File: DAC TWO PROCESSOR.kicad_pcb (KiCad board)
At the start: 4 copper layers, 94 x 50.8 mm, 100 parts, among them J1 CONN_20, J2 CONN_10x2, J3 CONN_10, U1 ADP5070, U10 LT1964-SD, U11 SM78L05, U12 SM79L05, U2 REG113-3.3, U3 XX MHz, U4 ADP7118, U5 AT25160B, U6 ADP7182, U7 STM32F7xx, U8 LT1763CS8, U9 LT1763CS8

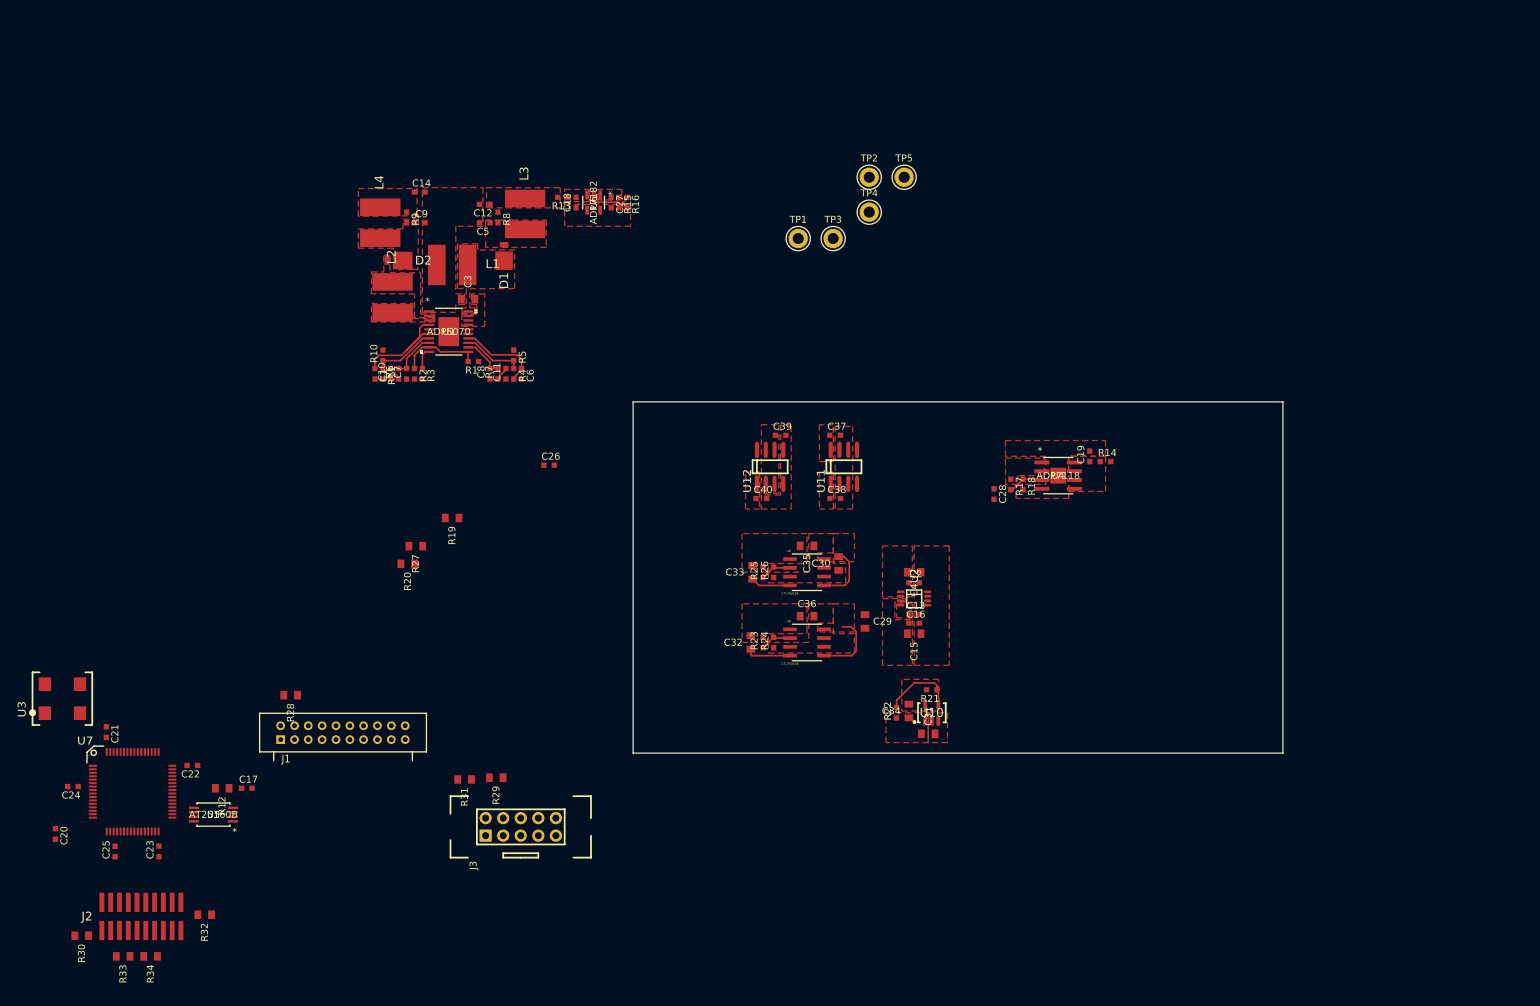
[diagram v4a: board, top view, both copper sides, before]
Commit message: Layout and placement of most switchers complete.
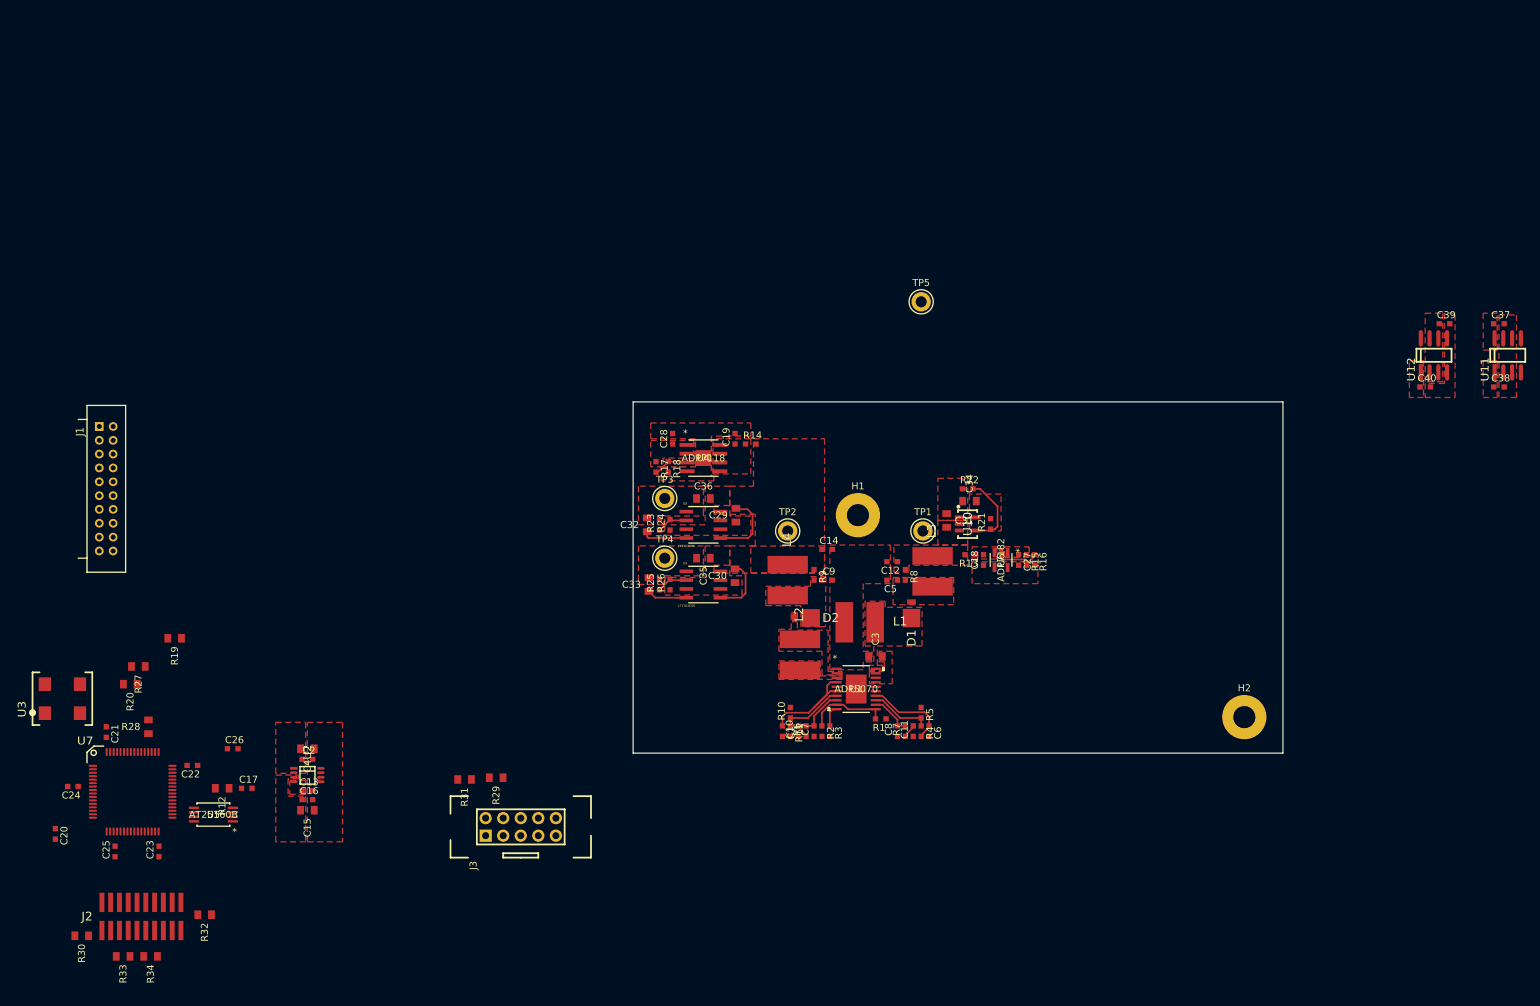
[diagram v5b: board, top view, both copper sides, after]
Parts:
- added H1: MountingHole_Pad, MountingHole:MountingHole_3.2mm_M3_Pad, F.Cu at (134.1, 102.7)
- added H2: MountingHole_Pad, MountingHole:MountingHole_3.2mm_M3_Pad, F.Cu at (190.0, 132.0)
- moved C37 97.4 mm to (226.8, 75.1)
- moved C38 97.4 mm to (226.8, 84.2)
- moved C39 97.4 mm to (218.9, 75.1)
- moved C40 97.4 mm to (216.2, 84.2)
- moved U11 97.4 mm to (228.1, 79.6)
- moved U12 97.4 mm to (217.4, 79.6)
- moved C13 91.4 mm to (54.5, 142.6)
- moved C15 91.4 mm to (54.5, 145.4)
- moved C16 91.4 mm to (54.5, 143.9)
- moved C2 91.4 mm to (54.5, 138.0)
- moved C4 91.4 mm to (54.5, 136.5)
- moved U2 91.4 mm to (54.5, 140.3)
- moved D1 78.4 mm to (141.9, 116.5)
- moved C27 78.4 mm to (157.4, 109.2)
- moved L1 78.4 mm to (134.4, 118.2)
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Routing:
- added copper zone on In1.Cu, net AGND

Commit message: EOD Commit
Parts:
- added C41: .1uF, SciMod:EIA0603, F.Cu at (108.3, 53.8)
- added C42: 10uF, SciMod:EIA3528, F.Cu at (96.3, 60.4)
- added C43: .1uF, SciMod:EIA0603, F.Cu at (102.2, 65.3)
- added C44: 10uF, SciMod:EIA3528, F.Cu at (106.2, 33.4)
- added C45: .1uF, SciMod:EIA0603, F.Cu at (107.5, 59.6)
- added C46: .1uF, SciMod:EIA0603, F.Cu at (102.2, 63.6)
- added C47: 10uF, SciMod:EIA3528, F.Cu at (98.4, 41.3)
- added C48: .1uF, SciMod:EIA0603, F.Cu at (108.4, 55.6)
- added C49: 10uF, SciMod:EIA3528, F.Cu at (90.2, 35.3)
- added C50: .1uF, SciMod:EIA0603, F.Cu at (89.0, 61.8)
- added C51: 10uF, SciMod:EIA0805, F.Cu at (75.4, 65.8)
- added C52: 10uF, SciMod:EIA3528, F.Cu at (90.9, 64.9)
- added C53: .1uF, SciMod:EIA0603, F.Cu at (115.0, 52.4)
- added C54: 10uF, SciMod:EIA3528, F.Cu at (103.7, 53.0)
- added C55: .1uF, SciMod:EIA0603, F.Cu at (112.3, 50.6)
- added C56: 10uF, SciMod:EIA3528, F.Cu at (102.9, 60.4)
- added C57: 1uF, SciMod:EIA0603, F.Cu at (95.5, 65.3)
- added C58: 47uF X7R, SciMod:EIA1210, F.Cu at (82.5, 65.3)
- added C59: 1uF, SciMod:EIA0603, F.Cu at (98.9, 63.6)
- added C60: .01uF, SciMod:EIA0603, F.Cu at (111.5, 48.9)
- added C61: 6800pF, SciMod:EIA0805, F.Cu at (89.4, 59.8)
- added C62: 6800pF, SciMod:EIA0805, F.Cu at (108.7, 51.8)
- added C63: 6800pF, SciMod:EIA0805, F.Cu at (81.9, 57.1)
- added C64: .1uF, SciMod:EIA0603, F.Cu at (111.8, 55.6)
- added C65: .1uF, SciMod:EIA0603, F.Cu at (95.5, 63.6)
- added C66: .1uF, SciMod:EIA0603, F.Cu at (111.5, 47.1)
- added C67: .1uF, SciMod:EIA0603, F.Cu at (114.8, 47.1)
- added H1, H2: MNT_HOLE, SciMod:HOLE188, F.Cu at (116.7, 168.0)
- added J4: FFC/ZIF, SciMod:MOLEX_52207-1233, F.Cu at (165.2, 94.6)
- added R35: 10K, SciMod:EIA0603, F.Cu at (105.1, 56.1)
- added R36: 10K, SciMod:EIA0603, F.Cu at (114.8, 48.9)
- added R37: 5K, SciMod:EIA0603, F.Cu at (107.5, 57.9)
- added R38, R40, R41: 33, SciMod:EIA0402, F.Cu at (116.7, 168.0)
- added R39: 10K, SciMod:EIA0603, F.Cu at (111.6, 53.8)
- added R42: 10K, SciMod:EIA0603, F.Cu at (115.6, 50.6)
- added R43: 10K, SciMod:EIA0603, F.Cu at (98.9, 65.3)
- added R44: 10K, SciMod:EIA0603, F.Cu at (110.8, 57.4)
- added R45: 30.1, SciMod:EIA0603, F.Cu at (101.8, 56.1)
- added R46: 30.1, SciMod:EIA0603, F.Cu at (107.5, 61.4)
- added R47: 0, SciMod:EIA0603, F.Cu at (105.5, 63.6)
- added R48: 0, SciMod:EIA0603, F.Cu at (110.8, 59.1)
- added R49: 0, SciMod:EIA0603, F.Cu at (114.1, 57.4)
- added R50: TBD, SciMod:SMR3D, F.Cu at (78.9, 54.0)
- added Rs1: TBD, SciMod:Z201, F.Cu at (116.7, 168.0)
- added TP7: VRN, SciMod:TESTPOINT, F.Cu at (78.5, 65.8)
- added U14: LT6655, SciMod:MSOP65P-8, F.Cu at (83.7, 61.1)
- added U15: AD5791ARUZ, SciMod:AD5791BRUZ, F.Cu at (98.4, 35.7)
- added U17: AD8675, SciMod:AD8675ARZ-REEL7, F.Cu at (88.6, 55.4)
- added U18: LTC2500, SciMod:LTC2500CDKD-32-TRPBF, F.Cu at (76.7, 60.4)
- added U20: OPA277, SciMod:SOIC127P-8, F.Cu at (97.0, 54.0)
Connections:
- J1 pad 16: (no net) -> SRGND
- U7 pad 10: (no net) -> MCLK
- U7 pad 11: (no net) -> SYNC
- U7 pad 15: (no net) -> PA1_NLDAC
- U7 pad 16: (no net) -> PA2_NCLR
- U7 pad 17: (no net) -> PA3_NRESET
- U7 pad 20: (no net) -> SPI1_NSS
- U7 pad 21: (no net) -> SPI1_SCK
- U7 pad 22: (no net) -> SPI1_MISO
- U7 pad 23: (no net) -> SPI1_MOSI
- U7 pad 24: (no net) -> BUSY
- U7 pad 37: (no net) -> DRL
- U7 pad 61: (no net) -> FPOS
- U7 pad 8: (no net) -> RDLA
- U7 pad 9: (no net) -> RDLB
